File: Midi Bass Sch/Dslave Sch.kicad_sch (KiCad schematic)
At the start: 12 parts, among them J5 D SLAVE ISCP, SW5 D-slave Reset, U7 PIC16F1789

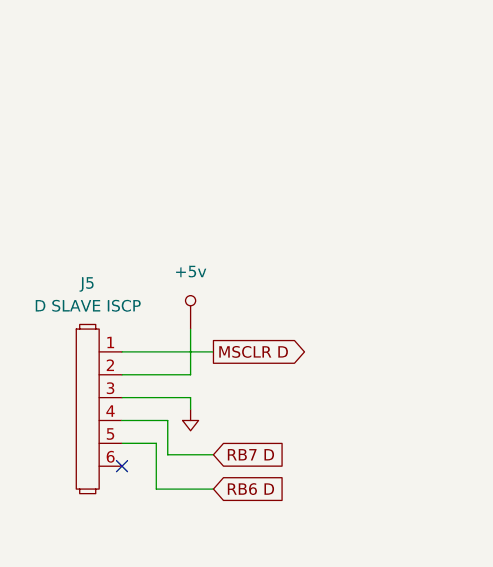
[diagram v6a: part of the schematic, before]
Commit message: started basic pcb layout for Master pic
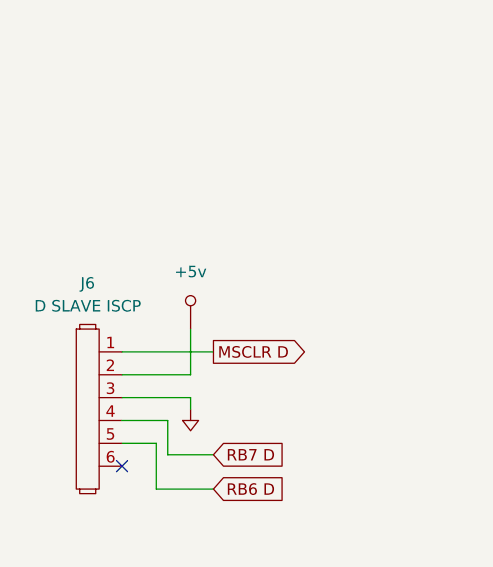
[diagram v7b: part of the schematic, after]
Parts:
- renumbered J5 to J6
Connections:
- net MSCLR D: now also D17.1; no longer D17.2
- net at C5.1, R51.1, SW5.2: now also D17.2; no longer D17.1
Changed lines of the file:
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@@
 		(dnp no)
 		(fields_autoplaced yes)
-		(property "Reference" "#PWR078"
+		(property "Reference" "#PWR080"
 			(at 190.5 124.46 0)
 			(effects
@@
 			(project "Midi Bass Sch"
 				(path "/06818073-fb22-48ee-acc5-6dedd827034e/4e89443f-252f-4d60-96aa-3cd5b0237902"
-					(reference "#PWR078")
+					(reference "#PWR080")
 					(unit 1)
 				)
@@
 		(dnp no)
 		(fields_autoplaced yes)
-		(property "Reference" "#PWR076"
+		(property "Reference" "#PWR078"
 			(at 110.1344 21.6916 0)
 			(effects
@@
 			(project "Midi Bass Sch"
 				(path "/06818073-fb22-48ee-acc5-6dedd827034e/4e89443f-252f-4d60-96aa-3cd5b0237902"
-					(reference "#PWR076")
+					(reference "#PWR078")
 					(unit 1)
 				)
@@
 		(dnp no)
 		(fields_autoplaced yes)
-		(property "Reference" "#PWR071"
+		(property "Reference" "#PWR073"
 			(at 40.2844 59.7916 0)
 			(effects
@@
 			(project "Midi Bass Sch"
 				(path "/06818073-fb22-48ee-acc5-6dedd827034e/4e89443f-252f-4d60-96aa-3cd5b0237902"
-					(reference "#PWR071")
+					(reference "#PWR073")
 					(unit 1)
 				)
@@
 		(dnp no)
 		(fields_autoplaced yes)
-		(property "Reference" "#PWR075"
+		(property "Reference" "#PWR077"
 			(at 102.87 158.75 0)
 			(effects
@@
 			(project "Midi Bass Sch"
 				(path "/06818073-fb22-48ee-acc5-6dedd827034e/4e89443f-252f-4d60-96aa-3cd5b0237902"
-					(reference "#PWR075")
+					(reference "#PWR077")
 					(unit 1)
 				)
@@
 		(dnp no)
 		(fields_autoplaced yes)
-		(property "Reference" "#PWR072"
+		(property "Reference" "#PWR074"
 			(at 35.56 72.39 0)
 			(effects
@@
 			(project "Midi Bass Sch"
 				(path "/06818073-fb22-48ee-acc5-6dedd827034e/4e89443f-252f-4d60-96aa-3cd5b0237902"
-					(reference "#PWR072")
+					(reference "#PWR074")
 					(unit 1)
 				)
@@
 		(dnp no)
 		(fields_autoplaced yes)
-		(property "Reference" "#PWR074"
+		(property "Reference" "#PWR076"
 			(at 48.26 139.7 0)
 			(effects
@@
 			(project "Midi Bass Sch"
 				(path "/06818073-fb22-48ee-acc5-6dedd827034e/4e89443f-252f-4d60-96aa-3cd5b0237902"
-					(reference "#PWR074")
+					(reference "#PWR076")
 					(unit 1)
 				)
@@
 		(dnp no)
 		(fields_autoplaced yes)
-		(property "Reference" "J5"
+		(property "Reference" "J6"
 			(at 24.13 59.69 0)
 			(effects
@@
 			(project "Midi Bass Sch"
 				(path "/06818073-fb22-48ee-acc5-6dedd827034e/4e89443f-252f-4d60-96aa-3cd5b0237902"
-					(reference "J5")
+					(reference "J6")
 					(unit 1)
 				)
@@
 		(dnp no)
 		(fields_autoplaced yes)
-		(property "Reference" "#PWR077"
+		(property "Reference" "#PWR079"
 			(at 176.53 127 0)
 			(effects
@@
 			(project "Midi Bass Sch"
 				(path "/06818073-fb22-48ee-acc5-6dedd827034e/4e89443f-252f-4d60-96aa-3cd5b0237902"
-					(reference "#PWR077")
+					(reference "#PWR079")
 					(unit 1)
 				)
@@
 		(dnp no)
 		(fields_autoplaced yes)
-		(property "Reference" "#PWR073"
+		(property "Reference" "#PWR075"
 			(at 52.9844 118.2116 0)
 			(effects
@@
 			(project "Midi Bass Sch"
 				(path "/06818073-fb22-48ee-acc5-6dedd827034e/4e89443f-252f-4d60-96aa-3cd5b0237902"
-					(reference "#PWR073")
+					(reference "#PWR075")
 					(unit 1)
 				)
@@
 		(dnp no)
 		(fields_autoplaced yes)
-		(property "Reference" "#PWR070"
+		(property "Reference" "#PWR072"
 			(at 26.67 140.97 0)
 			(effects
@@
 			(project "Midi Bass Sch"
 				(path "/06818073-fb22-48ee-acc5-6dedd827034e/4e89443f-252f-4d60-96aa-3cd5b0237902"
-					(reference "#PWR070")
-					(unit 1)
-				)
+					(reference "#PWR072")
+					(unit 1)
+				)

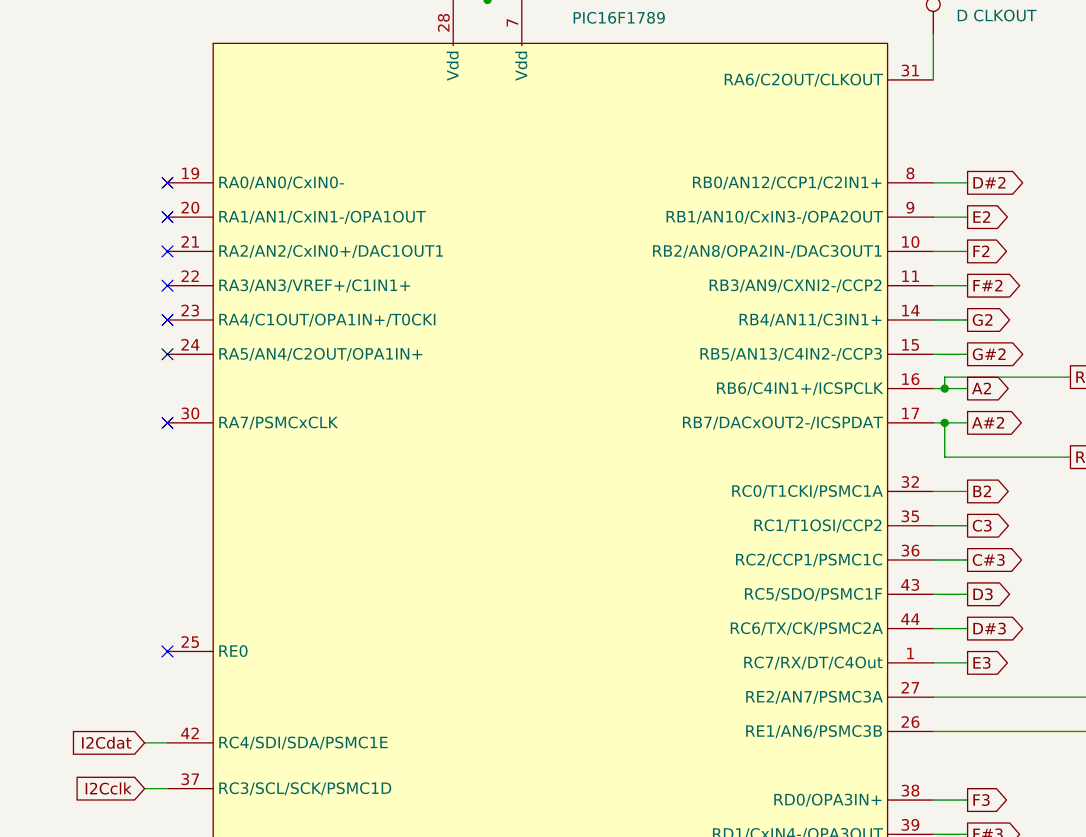
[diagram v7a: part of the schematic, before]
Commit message: updated schematic to reflect code
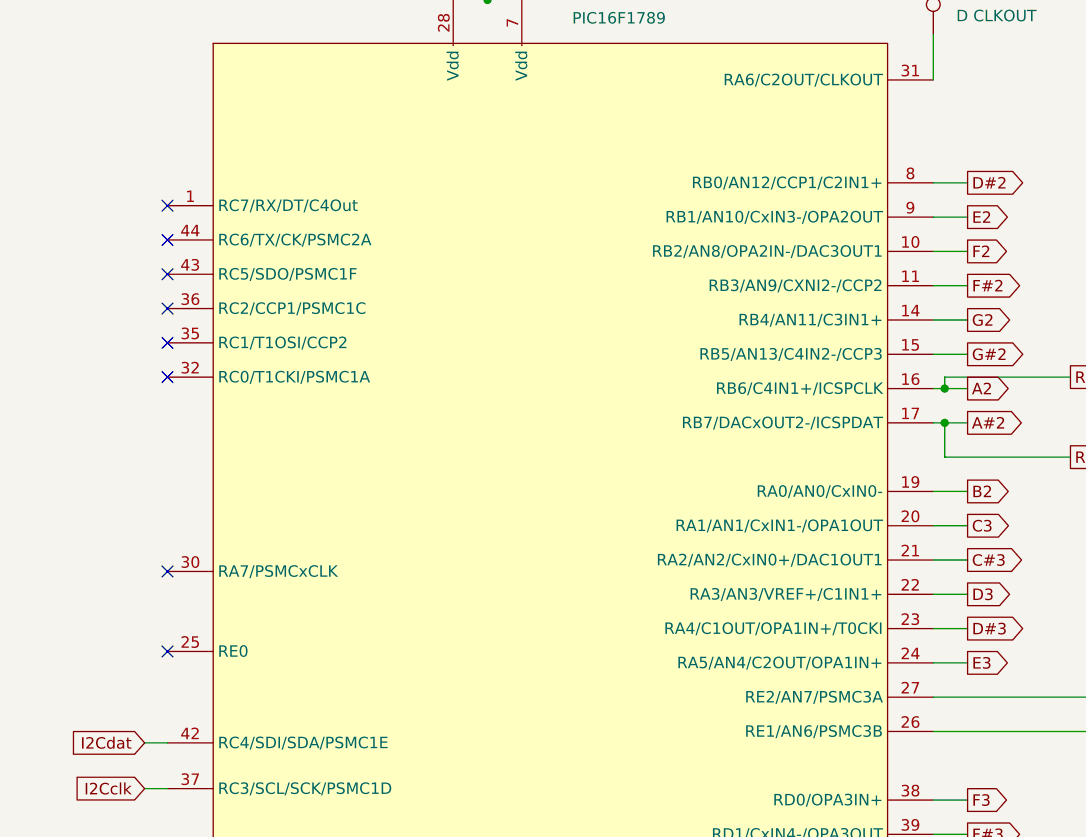
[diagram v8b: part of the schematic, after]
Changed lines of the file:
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@@
 	)
 	(no_connect
-		(at 69.85 59.69)
+		(at 69.85 62.23)
 	)
 	(no_connect
@@
 	)
 	(no_connect
-		(at 69.85 55.88)
+		(at 69.85 58.42)
 	)
 	(no_connect
-		(at 69.85 52.07)
+		(at 69.85 54.61)
 	)
 	(no_connect
-		(at 69.85 48.26)
+		(at 69.85 50.8)
 	)
 	(no_connect
@@
 	)
 	(no_connect
-		(at 69.85 67.31)
+		(at 69.85 69.85)
 	)
 	(no_connect
@@
 	)
 	(no_connect
-		(at 69.85 63.5)
+		(at 69.85 66.04)
 	)
 	(no_connect
-		(at 69.85 74.93)
+		(at 69.85 91.44)
 	)
 	(wire
